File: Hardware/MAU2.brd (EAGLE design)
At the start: 14 x 18 mm, 11 parts, among them IC1 BMP280, U1 ATTINY85-20SU-SOIC8

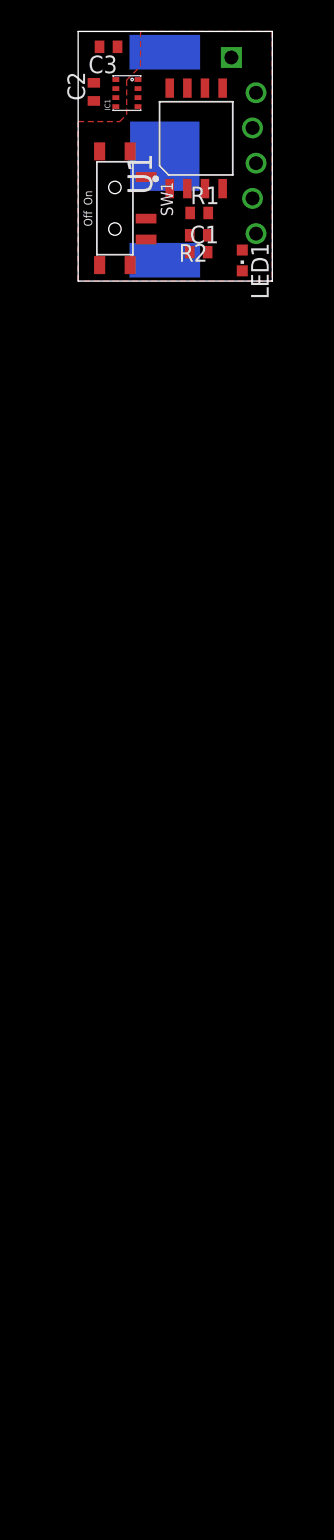
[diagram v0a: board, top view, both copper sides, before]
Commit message: MSP430 basic and USB connections (work in progress)
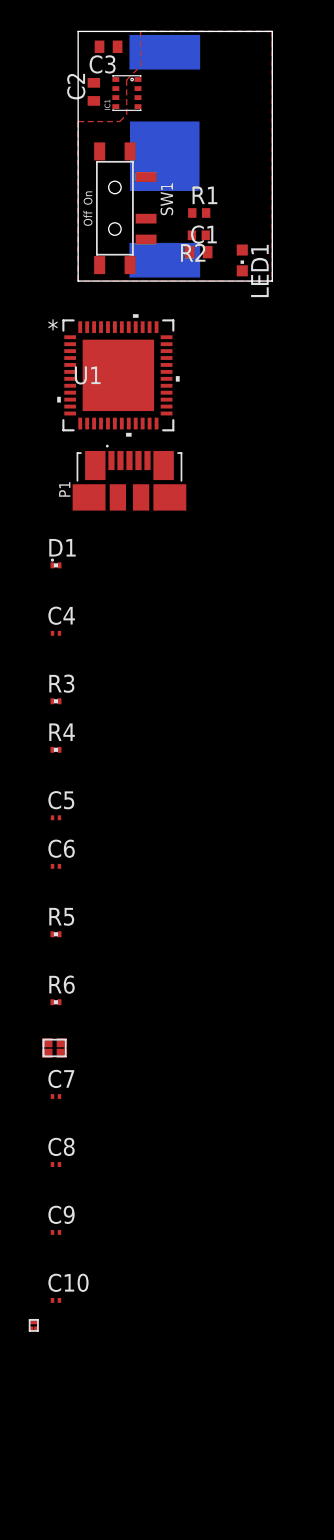
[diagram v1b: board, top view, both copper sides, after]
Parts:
- added C10, C9: 220nF, rcl:C0201
- added C4: 4.7uF, rcl:C0201
- added C5, C6, C7, C8: 10pF, rcl:C0201
- added D1: DIODE0201, GenericComponents:0201
- added P1: 47346-0001, MicroUSB:MOLEX_47346-0001
- added R3, R4: 27, rcl:R0201
- added R5, R6: 1.4k, rcl:R0201
- added XTAL_24MHZ: XTAL, GenericComponents:XTAL_SMD_1612
- R2: value 470 -> 100k
- U$1: value ISP_CONN_6_FDRILL16 -> MOSFET; device altimeter:ISP_CONN_6_F_DRILL16 -> GenericComponents:VLM0806
- U1: value ATTINY85-20SU-SOIC8 -> MSP430F5507IRGZR; device Seeed-OPL-ic:SOIC8-1.27-5.3X5.3MM -> Texas Instruments MCUs:RGZ48_5P15X5P15
- moved U$1 85.3 mm to (-3.20, -75.3)
- moved U1 18.0 mm to (2.90, -6.80)
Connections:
- new net AVCC1: U1.7
- new net AVSS1: U1.10
- new net AVSS2: U1.44
- new net DVCC1: U1.11
- new net DVCC2: U1.28
- new net DVSS1: U1.12
- new net DVSS2: U1.27
- new net N$10: R5.1, U1.39
- new net N$11: C8.2, U1.45, XTAL_24MHZ.P$1
- new net N$12: C7.1, U1.46, XTAL_24MHZ.P$3
- new net N$13: C9.1, U1.43
- new net N$14: C10.1, U1.42
- new net VCORE: U1.13
- net GND: now also C10.2, C4.2, C5.2, C6.2, C7.2, C8.1, C9.2, P1.5, P1.SH1, P1.SH2, P1.SH3, P1.SH4, P1.SH5, P1.SH6, R6.1, U1.37; no longer LED1.C, U$1.6, U1.4
- net N$2: now also C4.1, D1.1, U1.41; no longer R1.1, U1.2
- net N$3: now also D1.2, P1.1; no longer U$1.5, U1.1
- net N$5: now also C6.1, R3.1, U1.40; no longer IC1.2, U1.3
- net N$7: now also C5.1, R4.1, R5.2, R6.2, U1.38; no longer IC1.4, U$1.3, U1.7
- net N$8: now also P1.2, R3.2; no longer IC1.3, U$1.1, U1.6
- net N$9: now also P1.3, R4.2; no longer IC1.5, U$1.4, U1.5
- net VCC: no longer U$1.2, U1.8

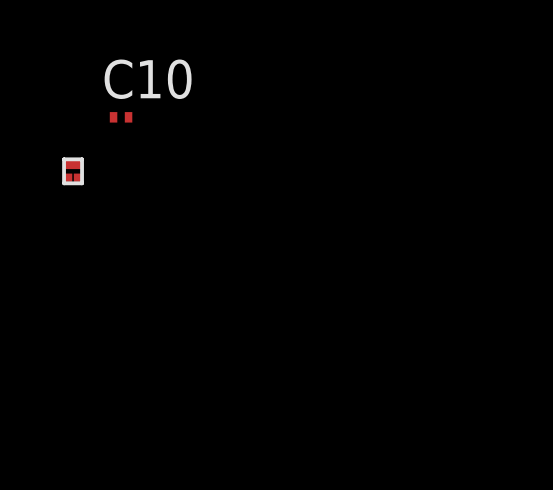
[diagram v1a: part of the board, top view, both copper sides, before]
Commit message: Schematics complete
Added connections between MOSFET and DVcc;
Added SPI connections between MSP430 and BMP280;
Added connection between LED and MSP430.
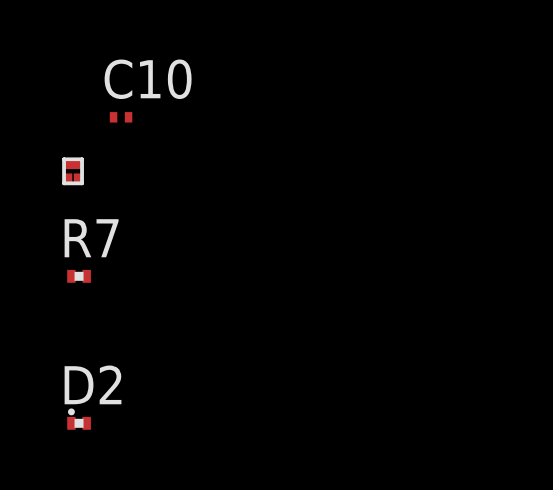
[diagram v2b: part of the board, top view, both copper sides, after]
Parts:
- added D2: DIODE0201, GenericComponents:0201
- added R7: 100k, rcl:R0201
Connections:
- removed net DVCC1: U1.11
- removed net DVCC2: U1.28
- removed net DVSS1: U1.12
- removed net DVSS2: U1.27
- new net N$15: R7.1, U$1.P$1
- new net N$16: IC1.5, U1.34
- new net N$17: C1.1, D2.1, U$1.P$3, U1.11, U1.28
- new net N$18: IC1.3, U1.33
- new net N$19: IC1.4, U1.29
- new net N$20: IC1.2, U1.1
- new net N$21: R1.1, U1.2
- net GND: now also LED1.C, U1.12, U1.27
- net N$14: now also D2.2
- net N$3: now also R7.2
- net VCC: now also U$1.P$2; no longer C1.1
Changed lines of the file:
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@@
 </element>
 <element name="U$1" library="GenericComponents" package="VLM0806" value="MOSFET" x="-3.2" y="-75.3"/>
+<element name="R7" library="rcl" library_urn="urn:adsk.eagle:library:334" package="R0201" package3d_urn="urn:adsk.eagle:package:23593/1" value="100k" x="-3" y="-78.8">
+<attribute name="SPICEPREFIX" value="R" x="-3" y="-78.8" size="1.778" layer="27" display="off"/>
+</element>
+<element name="D2" library="GenericComponents" package="0201" value="DIODE0201" x="-3" y="-83.7"/>
 </elements>
 <signals>
 <signal name="VCC">
-<contactref element="C1" pad="1"/>
 <contactref element="C2" pad="1"/>
 <contactref element="IC1" pad="8"/>
@@
 </polygon>
 <contactref element="R2" pad="1"/>
-<wire x1="2.8424" y1="16.891" x2="6.25" y2="16.5" width="0" layer="19" extent="1-16"/>
-<wire x1="2.717" y1="14.53" x2="2.8424" y2="16.891" width="0" layer="19" extent="1-1"/>
-<wire x1="2.717" y1="13.23" x2="2.717" y2="14.53" width="0" layer="19" extent="1-1"/>
-<wire x1="1.134" y1="12.9898" x2="2.717" y2="13.23" width="0" layer="19" extent="1-1"/>
-<wire x1="1.55" y1="9.35" x2="1.134" y2="12.9898" width="0" layer="19" extent="1-1"/>
-<wire x1="3.75" y1="9.35" x2="1.55" y2="9.35" width="0" layer="19" extent="1-1"/>
-<wire x1="3.75" y1="1.15" x2="3.75" y2="9.35" width="0" layer="19" extent="1-1"/>
-<wire x1="1.55" y1="1.15" x2="3.75" y2="1.15" width="0" layer="19" extent="1-1"/>
+<contactref element="U$1" pad="P$2"/>
+<wire x1="1.55" y1="1.15" x2="-3.025" y2="-75.55" width="0" layer="19" extent="1-1"/>
+<wire x1="3.75" y1="1.15" x2="1.55" y2="1.15" width="0" layer="19" extent="1-1"/>
 <wire x1="6.25" y1="1.5" x2="3.75" y2="1.15" width="0" layer="19" extent="1-16"/>
-<wire x1="8.036" y1="2.084" x2="6.25" y2="1.5" width="0" layer="19" extent="1-16"/>
-<wire x1="9.2" y1="3.3" x2="8.036" y2="2.084" width="0" layer="19" extent="1-1"/>
+<wire x1="9.2" y1="3.3" x2="6.25" y2="1.5" width="0" layer="19" extent="1-16"/>
+<wire x1="3.75" y1="9.35" x2="9.2" y2="3.3" width="0" layer="19" extent="1-1"/>
+<wire x1="1.55" y1="9.35" x2="3.75" y2="9.35" width="0" layer="19" extent="1-1"/>
+<wire x1="1.134" y1="12.9898" x2="1.55" y2="9.35" width="0" layer="19" extent="1-1"/>
+<wire x1="2.717" y1="13.23" x2="1.134" y2="12.9898" width="0" layer="19" extent="1-1"/>
+<wire x1="2.717" y1="14.53" x2="2.717" y2="13.23" width="0" layer="19" extent="1-1"/>
+<wire x1="2.8424" y1="16.891" x2="2.717" y2="14.53" width="0" layer="19" extent="1-1"/>
+<wire x1="6.25" y1="16.5" x2="2.8424" y2="16.891" width="0" layer="19" extent="1-16"/>
 </signal>
 <signal name="GND">
@@
 <contactref element="P1" pad="SH6"/>
 <contactref element="P1" pad="SH3"/>
+<contactref element="U1" pad="12"/>
+<contactref element="U1" pad="27"/>
+<contactref element="LED1" pad="C"/>
 <wire x1="-1.35" y1="-68.6" x2="-1.35" y2="-73.5" width="0" layer="19" extent="1-1"/>
 <wire x1="-1.85" y1="-63.7" x2="-1.35" y2="-68.6" width="0" layer="19" extent="1-1"/>
@@
 <wire x1="6.1625" y1="-13.3" x2="6.6125" y2="-15.6" width="0" layer="19" extent="1-1"/>
 <wire x1="5" y1="-12.94" x2="6.1625" y2="-13.3" width="0" layer="19" extent="1-1"/>
-<wire x1="5.65069375" y1="-3.325" x2="5" y2="-12.94" width="0" layer="19" extent="1-1"/>
+<wire x1="-0.575" y1="-9.55" x2="1.2375" y2="-13.3" width="0" layer="19" extent="1-1"/>
+<wire x1="6.375" y1="-8.55" x2="5" y2="-12.94" width="0" layer="19" extent="1-1"/>
+<wire x1="5.65069375" y1="-3.325" x2="6.375" y2="-8.55" width="0" layer="19" extent="1-1"/>
 <wire x1="9.336" y1="2.084" x2="5.65069375" y2="-3.325" width="0" layer="19" extent="1-1"/>
+<wire x1="11.836" y1="0.7376" x2="9.336" y2="2.084" width="0" layer="19" extent="1-1"/>
 <wire x1="4.9" y1="4.5" x2="9.336" y2="2.084" width="0" layer="19" extent="1-1"/>
 <wire x1="2.717" y1="13.88" x2="4.9" y2="4.5" width="0" layer="19" extent="1-1"/>
@@
 <wire x1="1.5424" y1="16.891" x2="1.134" y2="14.2898" width="0" layer="19" extent="1-1"/>
 </signal>
-<signal name="N$4">
-<contactref element="R1" pad="2"/>
-<contactref element="LED1" pad="A"/>
-<wire x1="11.836" y1="2.2376" x2="9.228" y2="4.91" width="0" layer="19" extent="1-1"/>
-</signal>
 <signal name="N$1">
 <contactref element="G1" pad="-"/>
@@
 <contactref element="U1" pad="10"/>
 </signal>
-<signal name="DVCC1">
-<contactref element="U1" pad="11"/>
-</signal>
-<signal name="DVSS1">
-<contactref element="U1" pad="12"/>
-</signal>
 <signal name="VCORE">
 <contactref element="U1" pad="13"/>
-</signal>
-<signal name="DVSS2">
-<contactref element="U1" pad="27"/>
-</signal>
-<signal name="DVCC2">
-<contactref element="U1" pad="28"/>
 </signal>
 <signal name="AVSS2">
@@
 <contactref element="P1" pad="1"/>
 <contactref element="D1" pad="2"/>
+<contactref element="R7" pad="2"/>
+<wire x1="-1.345" y1="-20.5" x2="-2.745" y2="-78.8" width="0" layer="19" extent="1-1"/>
 <wire x1="2.4" y1="-12.94" x2="-1.345" y2="-20.5" width="0" layer="19" extent="1-1"/>
 </signal>
@@
 <contactref element="U1" pad="42"/>
 <contactref element="C10" pad="1"/>
+<contactref element="D2" pad="2"/>
+<wire x1="-1.85" y1="-73.5" x2="-2.745" y2="-83.7" width="0" layer="19" extent="1-1"/>
 <wire x1="3.1500625" y1="-3.325" x2="-1.85" y2="-73.5" width="0" layer="19" extent="1-1"/>
 </signal>
+<signal name="N$15">
+<contactref element="U$1" pad="P$1"/>
+<contactref element="R7" pad="1"/>
+<wire x1="-3.375" y1="-75.55" x2="-3.255" y2="-78.8" width="0" layer="19" extent="1-1"/>
+</signal>
+<signal name="N$17">
+<contactref element="U$1" pad="P$3"/>
+<contactref element="U1" pad="11"/>
+<contactref element="C1" pad="1"/>
+<contactref element="D2" pad="1"/>
+<contactref element="U1" pad="28"/>
+<wire x1="-3.2" y1="-75.05" x2="-3.255" y2="-83.7" width="0" layer="19" extent="1-1"/>
+<wire x1="-0.575" y1="-9.05" x2="-3.2" y2="-75.05" width="0" layer="19" extent="1-1"/>
+<wire x1="6.375" y1="-8.05" x2="-0.575" y2="-9.05" width="0" layer="19" extent="1-1"/>
+<wire x1="8.036" y1="2.084" x2="6.375" y2="-8.05" width="0" layer="19" extent="1-1"/>
+</signal>
+<signal name="N$16">
+<contactref element="IC1" pad="5"/>
+<contactref element="U1" pad="34"/>
+<wire x1="6.375" y1="-5.05" x2="2.717" y2="12.58" width="0" layer="19" extent="1-1"/>
+</signal>
+<signal name="N$18">
+<contactref element="IC1" pad="3"/>
+<contactref element="U1" pad="33"/>
+<wire x1="6.375" y1="-5.55" x2="4.317" y2="13.23" width="0" layer="19" extent="1-1"/>
+</signal>
+<signal name="N$19">
+<contactref element="IC1" pad="4"/>
+<contactref element="U1" pad="29"/>
+<wire x1="6.375" y1="-7.55" x2="4.317" y2="12.58" width="0" layer="19" extent="1-1"/>
+</signal>
+<signal name="N$20">
+<contactref element="IC1" pad="2"/>
+<contactref element="U1" pad="1"/>
+<wire x1="-0.575" y1="-4.05" x2="4.317" y2="13.88" width="0" layer="19" extent="1-1"/>
+</signal>
+<signal name="N$21">
+<contactref element="U1" pad="2"/>
+<contactref element="R1" pad="1"/>
+<wire x1="-0.575" y1="-4.55" x2="8.228" y2="4.91" width="0" layer="19" extent="1-1"/>
+</signal>
+<signal name="N$4">
+<contactref element="R1" pad="2"/>
+<contactref element="LED1" pad="A"/>
+<wire x1="11.836" y1="2.2376" x2="9.228" y2="4.91" width="0" layer="19" extent="1-1"/>
+</signal>
 </signals>

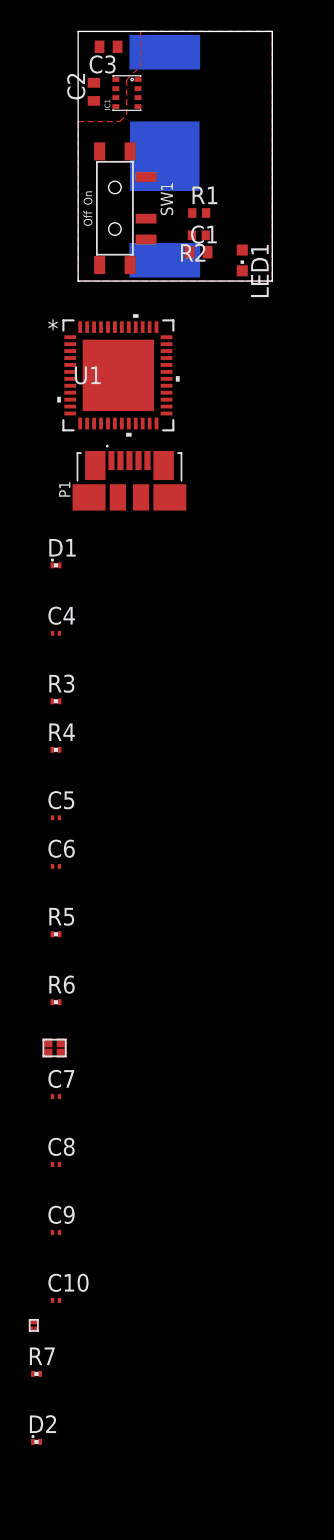
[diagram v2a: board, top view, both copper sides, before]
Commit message: All CPU needed pins connected and CPU positioned in the board
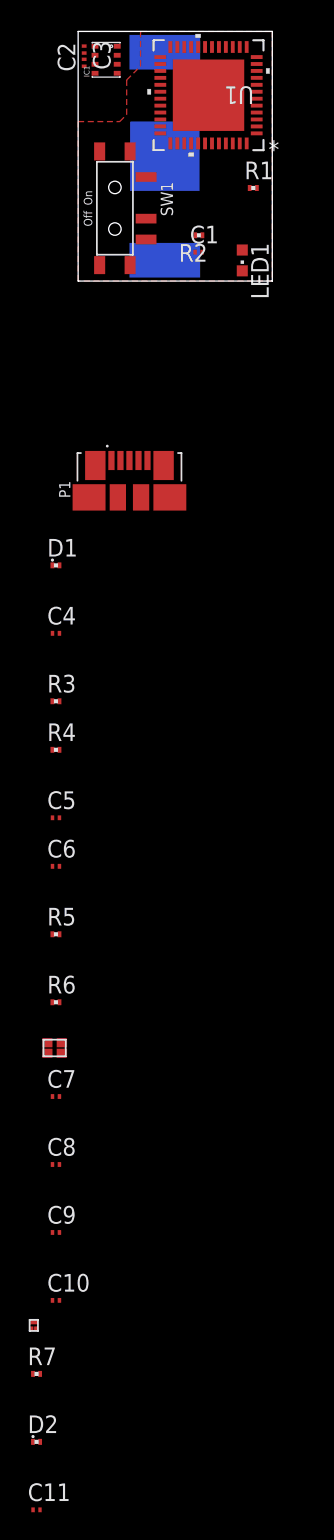
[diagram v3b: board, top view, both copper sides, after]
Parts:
- added C11: 10nF, rcl:C0201
- C1, C2, C3: device rcl:C0402 -> rcl:C0201
- R1, R2: device rcl:R0402 -> rcl:R0201
- moved U1 21.2 mm to (9.40, 13.4), turned to 180 degrees
- moved R1 4.30 mm to (12.6, 6.71)
- moved IC1 2.83 mm to (2.02, 16.0)
- moved C2 2.21 mm to (0.43, 15.7)
- moved C3 1.77 mm to (0.43, 16.7), turned to 270 degrees
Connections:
- removed net AVCC1: U1.7
- removed net AVSS1: U1.10
- removed net AVSS2: U1.44
- new net VCC-FET: C1.1, D2.1, U$1.P$3, U1.11, U1.28, U1.7
- net GND: now also C11.2, U1.10, U1.44, U1.49
- net N$17: now also C11.1, U1.48; no longer C1.1, D2.1, U$1.P$3, U1.11, U1.28
- net N$20: now also U1.25; no longer U1.1
- net N$21: now also U1.1; no longer U1.2

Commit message: All components positioned
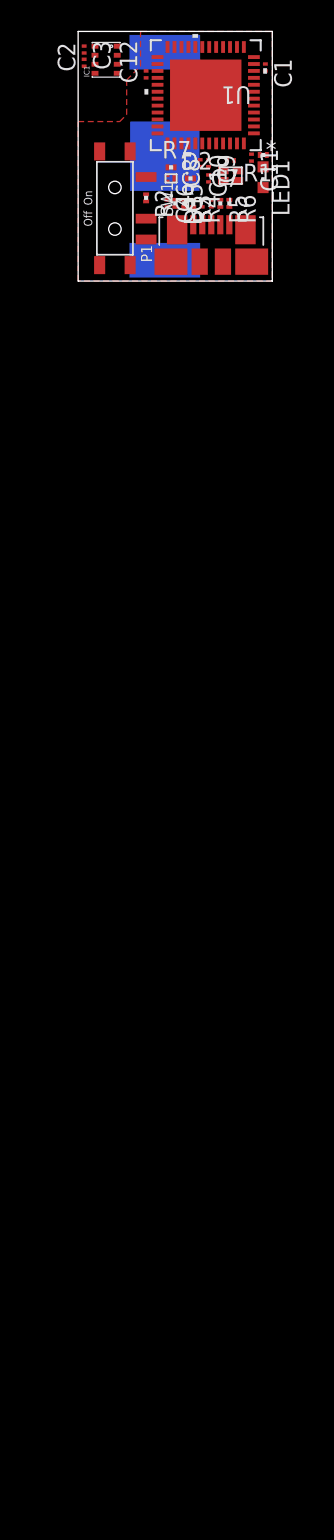
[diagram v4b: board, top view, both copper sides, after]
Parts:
- added C12: 1uF, rcl:C0201
- R6: value 1.4k -> 1M
- moved C11 98.7 mm to (12.5, 8.90), turned to 270 degrees
- moved D2 91.8 mm to (8.10, 7.40)
- moved R7 87.5 mm to (6.70, 8.20)
- moved U$1 83.3 mm to (6.70, 7.40), turned to 270 degrees
- moved C10 82.7 mm to (8.80, 8.50), turned to 270 degrees
- moved C9 77.9 mm to (9.40, 8.50), turned to 270 degrees
- moved C8 71.9 mm to (9.40, 7.40), turned to 90 degrees
- moved C7 68.7 mm to (11.0, 8.70), turned to 180 degrees
- moved XTAL_24MHZ 64.2 mm to (11.0, 7.60)
- moved R6 58.9 mm to (10.9, 5.60), turned to 270 degrees
- moved R5 54.0 mm to (10.2, 5.60), turned to 270 degrees
- moved C6 49.0 mm to (8.95, 5.60), turned to 90 degrees
- moved C5 45.7 mm to (9.60, 5.60), turned to 90 degrees
- moved R4 40.6 mm to (8.30, 5.60), turned to 270 degrees
- moved R3 37.1 mm to (7.65, 5.60), turned to 270 degrees
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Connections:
- net GND: now also C12.2
- net VCC-FET: now also C12.1

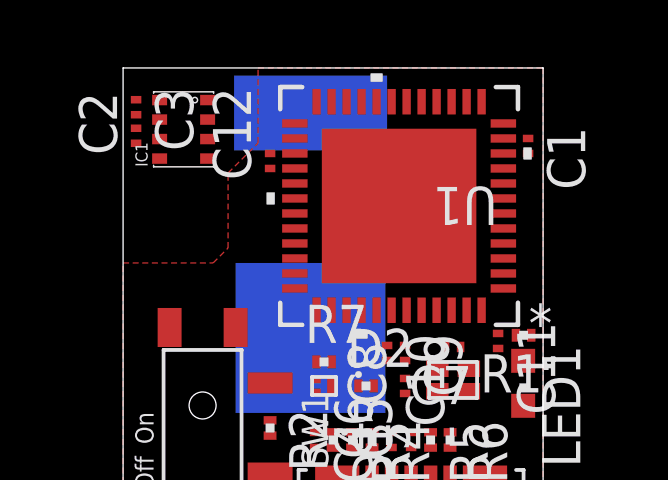
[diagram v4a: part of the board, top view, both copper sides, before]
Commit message: Ratsnet Polygon updated to cover the whole board
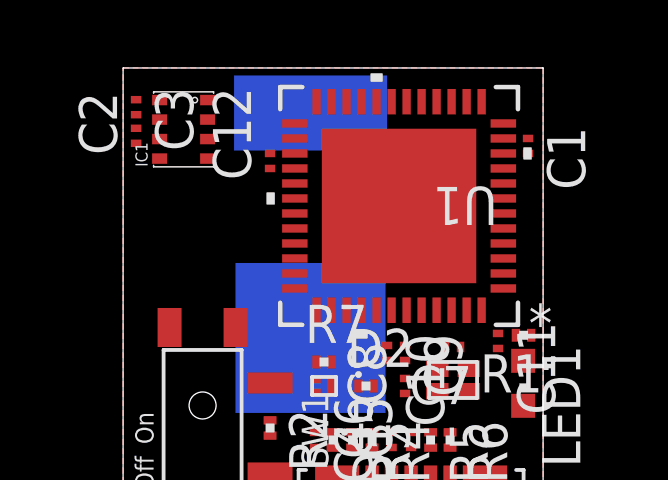
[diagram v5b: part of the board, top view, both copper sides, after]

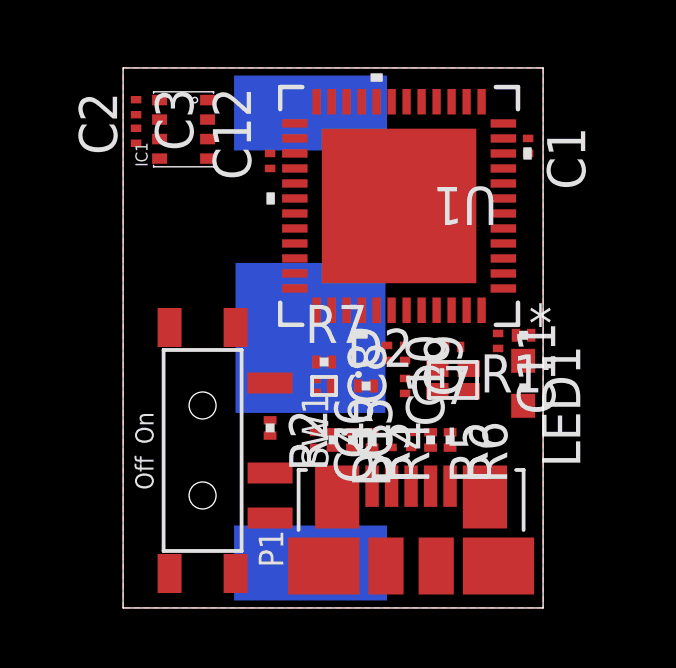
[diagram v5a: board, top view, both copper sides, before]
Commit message: Routing in progress, set BMP280 supply to VCC-FET
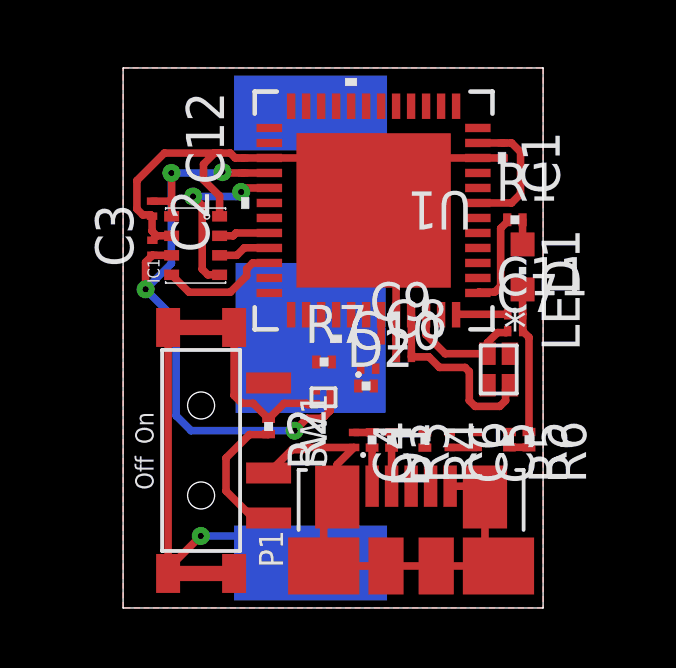
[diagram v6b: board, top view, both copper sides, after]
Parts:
- moved C3 4.72 mm to (0.98, 12.0), turned to 90 degrees
- moved IC1 3.90 mm to (2.42, 12.1)
- moved LED1 3.88 mm to (13.3, 11.4)
- moved R1 3.86 mm to (13.1, 12.9), turned to 0 degrees
- moved R5 2.63 mm to (12.9, 5.61)
- moved R6 2.63 mm to (13.5, 5.61)
- moved C2 2.49 mm to (0.97, 13.3), turned to 270 degrees
- moved C5 2.19 mm to (11.8, 5.60), turned to 270 degrees
- moved C7 2.14 mm to (13.1, 9.23), turned to 0 degrees
- moved C6 1.94 mm to (10.9, 5.60), turned to 270 degrees
- moved R4 1.76 mm to (10.1, 5.60)
- moved XTAL_24MHZ 1.56 mm to (12.5, 7.95), turned to 90 degrees
- moved D1 1.30 mm to (8.30, 5.60)
- moved C4 1.30 mm to (7.70, 5.60)
- moved R3 1.30 mm to (8.95, 5.60)
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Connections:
- net N$20: now also U1.32; no longer U1.25
- net VCC: no longer C2.1, C3.1, IC1.6, IC1.8
- net VCC-FET: now also C2.1, C3.1, IC1.6, IC1.8
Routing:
- net GND: track 0.00 -> 48.1 mm
- net VCC-FET: track 0.00 -> 26.7 mm, vias 0 -> 4
- net VCC: track 0.00 -> 23.9 mm, vias 0 -> 1
- net N$11: track 0.00 -> 6.45 mm
- net N$19: track 0.00 -> 5.86 mm, vias 0 -> 2
- net N$6: track 0.00 -> 4.64 mm
- net N$12: track 0.00 -> 4.18 mm
- net N$16: track 0.00 -> 4.04 mm
- net N$21: track 0.00 -> 3.16 mm
- net N$18: track 0.00 -> 1.76 mm
- net N$17: track 0.00 -> 1.73 mm
- net N$20: track 0.00 -> 1.70 mm
- net N$8: track 0.00 -> 1.29 mm
- net N$22: track 0.00 -> 1.29 mm
- net N$13: track 0.00 -> 0.83 mm
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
